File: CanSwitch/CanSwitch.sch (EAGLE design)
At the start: 17 parts

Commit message: #11 fixing RJ45 connector - connecting unused pins to +5V and GND
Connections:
- net +5V: now also RJ45CONNECTOR.RJ4515, RJ45CONNECTOR.RJ4517, RJ45CONNECTOR.RJ4525, RJ45CONNECTOR.RJ4527
- net GND: now also RJ45CONNECTOR.RJ4516, RJ45CONNECTOR.RJ4526
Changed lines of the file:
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@@
 <?xml version="1.0" encoding="utf-8"?>
 <!DOCTYPE eagle SYSTEM "eagle.dtd">
-<eagle version="7.6.0">
+<eagle version="7.7.0">
 <drawing>
 <settings>
@@
 <part name="STATUSLED" library="led" deviceset="LED" device="5MM"/>
 <part name="GND7" library="supply1" deviceset="GND" device=""/>
-<part name="GND1" library="supply1" deviceset="GND" device=""/>
 <part name="P+1" library="supply1" deviceset="+5V" device=""/>
 <part name="GND3" library="supply1" deviceset="GND" device=""/>
@@
 <instance part="STATUSLED" gate="G$1" x="-121.92" y="76.2" rot="R90"/>
 <instance part="GND7" gate="1" x="-134.62" y="76.2" rot="R270"/>
-<instance part="GND1" gate="1" x="-53.34" y="111.76"/>
 <instance part="P+1" gate="1" x="-27.94" y="91.44" rot="R90"/>
 <instance part="GND3" gate="1" x="-27.94" y="104.14" rot="R270"/>
@@
 </segment>
 <segment>
-<pinref part="RJ45CONNECTOR" gate="G$1" pin="RJ4519"/>
-<wire x1="-60.96" y1="119.38" x2="-55.88" y2="119.38" width="0.1524" layer="91"/>
-<label x="-60.96" y="116.84" size="1.778" layer="95"/>
-</segment>
-<segment>
 <pinref part="RJ45CONNECTOR" gate="G$1" pin="RJ4529"/>
 <wire x1="-20.32" y1="119.38" x2="-5.08" y2="119.38" width="0.1524" layer="91"/>
@@
 <wire x1="-48.26" y1="53.34" x2="-60.96" y2="53.34" width="0.1524" layer="91"/>
 <label x="-60.96" y="53.34" size="1.778" layer="95"/>
+</segment>
+<segment>
+<pinref part="RJ45CONNECTOR" gate="G$1" pin="RJ4515"/>
+<wire x1="-91.44" y1="119.38" x2="-104.14" y2="119.38" width="0.1524" layer="91"/>
+<label x="-106.68" y="119.38" size="1.778" layer="95"/>
+</segment>
+<segment>
+<pinref part="RJ45CONNECTOR" gate="G$1" pin="RJ4527"/>
+<wire x1="-20.32" y1="127" x2="-5.08" y2="127" width="0.1524" layer="91"/>
+<label x="-10.16" y="127" size="1.778" layer="95"/>
+</segment>
+<segment>
+<pinref part="RJ45CONNECTOR" gate="G$1" pin="RJ4517"/>
+<wire x1="-60.96" y1="127" x2="-58.42" y2="127" width="0.1524" layer="91"/>
+<label x="-63.5" y="124.46" size="1.778" layer="95"/>
+</segment>
+<segment>
+<pinref part="RJ45CONNECTOR" gate="G$1" pin="RJ4519"/>
+<pinref part="RJ45CONNECTOR" gate="G$1" pin="RJ4525"/>
+<wire x1="-60.96" y1="119.38" x2="-50.8" y2="119.38" width="0.1524" layer="91"/>
+<label x="-58.42" y="116.84" size="1.778" layer="95"/>
 </segment>
 </net>
@@
 </segment>
 <segment>
-<pinref part="RJ45CONNECTOR" gate="G$1" pin="RJ4518"/>
-<pinref part="RJ45CONNECTOR" gate="G$1" pin="RJ4524"/>
-<wire x1="-50.8" y1="121.92" x2="-53.34" y2="121.92" width="0.1524" layer="91"/>
-<pinref part="GND1" gate="1" pin="GND"/>
-<wire x1="-53.34" y1="121.92" x2="-60.96" y2="121.92" width="0.1524" layer="91"/>
-<wire x1="-53.34" y1="114.3" x2="-53.34" y2="121.92" width="0.1524" layer="91"/>
-<junction x="-53.34" y="121.92"/>
-</segment>
-<segment>
 <pinref part="DEBUGGING" gate="A" pin="3"/>
 <wire x1="-48.26" y1="50.8" x2="-60.96" y2="50.8" width="0.1524" layer="91"/>
 <label x="-60.96" y="50.8" size="1.778" layer="95"/>
+</segment>
+<segment>
+<pinref part="RJ45CONNECTOR" gate="G$1" pin="RJ4518"/>
+<pinref part="RJ45CONNECTOR" gate="G$1" pin="RJ4524"/>
+<wire x1="-50.8" y1="121.92" x2="-60.96" y2="121.92" width="0.1524" layer="91"/>
+<label x="-58.42" y="121.92" size="1.778" layer="95"/>
+</segment>
+<segment>
+<pinref part="RJ45CONNECTOR" gate="G$1" pin="RJ4526"/>
+<wire x1="-20.32" y1="129.54" x2="-5.08" y2="129.54" width="0.1524" layer="91"/>
+<label x="-10.16" y="129.54" size="1.778" layer="95"/>
+</segment>
+<segment>
+<pinref part="RJ45CONNECTOR" gate="G$1" pin="RJ4516"/>
+<wire x1="-60.96" y1="129.54" x2="-58.42" y2="129.54" width="0.1524" layer="91"/>
+<label x="-63.5" y="132.08" size="1.778" layer="95"/>
 </segment>
 </net>
@@
 <segment>
 <pinref part="RJ45CONNECTOR" gate="G$1" pin="RJ4522"/>
-<wire x1="-50.8" y1="129.54" x2="-58.42" y2="129.54" width="0.1524" layer="91"/>
-<label x="-58.42" y="132.08" size="1.778" layer="95"/>
+<wire x1="-50.8" y1="129.54" x2="-53.34" y2="129.54" width="0.1524" layer="91"/>
+<label x="-55.88" y="132.08" size="1.778" layer="95"/>
 </segment>
 </net>
@@
 <segment>
 <pinref part="RJ45CONNECTOR" gate="G$1" pin="RJ4523"/>
-<wire x1="-58.42" y1="127" x2="-50.8" y2="127" width="0.1524" layer="91"/>
-<label x="-58.42" y="124.46" size="1.778" layer="95"/>
-</segment>
-<segment>
+<wire x1="-53.34" y1="127" x2="-50.8" y2="127" width="0.1524" layer="91"/>
+<label x="-55.88" y="124.46" size="1.778" layer="95"/>
+</segment>
+<segment>

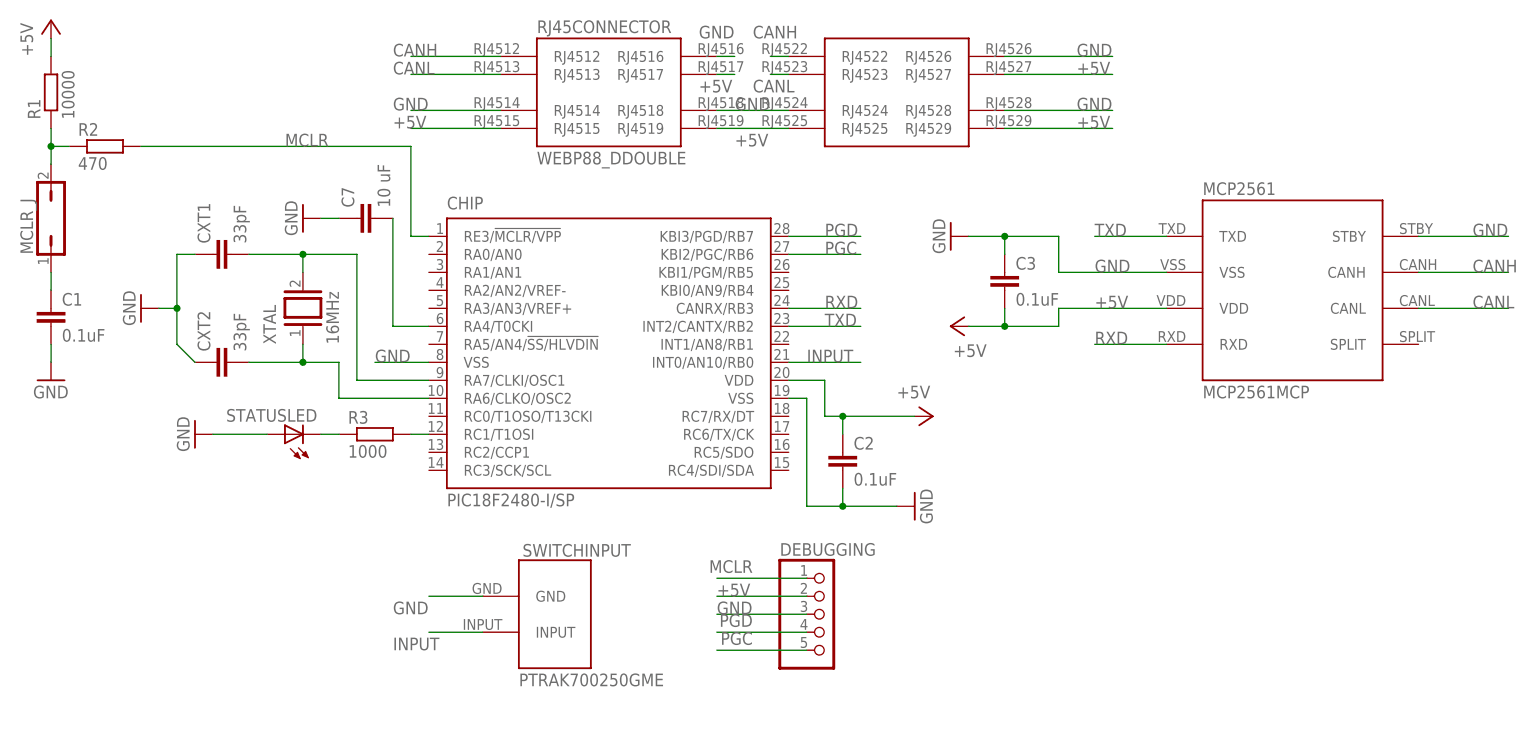
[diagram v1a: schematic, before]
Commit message: #13 connect RC3 of chip and STBY of transceiver, no route yet in board until the new inputs are added
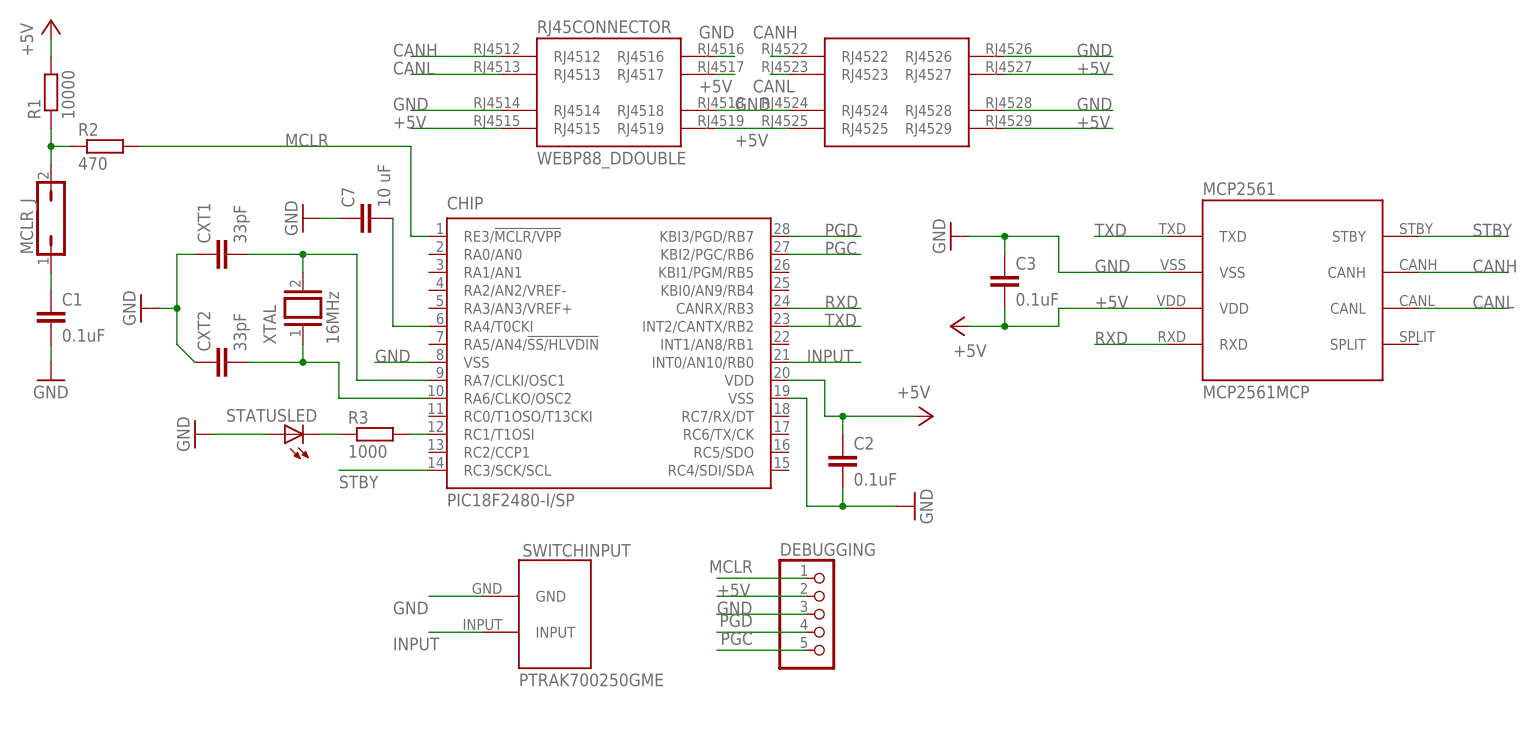
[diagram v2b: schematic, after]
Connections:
- new net STBY: CHIP.RC3/SCK/SCL, MCP2561.STBY
- net GND: no longer MCP2561.STBY
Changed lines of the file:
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@@
-</segment>
-<segment>
-<pinref part="MCP2561" gate="G$1" pin="STBY"/>
-<wire x1="38.1" y1="104.14" x2="50.8" y2="104.14" width="0.1524" layer="91"/>
-<label x="45.72" y="104.14" size="1.778" layer="95"/>
 </segment>
 <segment>
@@
 </segment>
 </net>
+<net name="STBY" class="0">
+<segment>
+<pinref part="MCP2561" gate="G$1" pin="STBY"/>
+<wire x1="38.1" y1="104.14" x2="50.8" y2="104.14" width="0.1524" layer="91"/>
+<label x="45.72" y="104.14" size="1.778" layer="95"/>
+</segment>
+<segment>
+<pinref part="CHIP" gate="G$1" pin="RC3/SCK/SCL"/>
+<wire x1="-101.6" y1="71.12" x2="-114.3" y2="71.12" width="0.1524" layer="91"/>
+<label x="-114.3" y="68.58" size="1.778" layer="95"/>
+</segment>
+</net>

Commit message: #8 support for 8 independent inputs  - dropped old switch input and replaced with RJ45 connector  - moved components around, moved transceiver down to the bottom and the  new RJ45 in the middle close to the chip  - re-routed related signals, made +5V thicker  - RX and TX routed to RC pins afterall, added labels too  - Eagle now reports clearance on the RJ45 socket, need to check allpcb  whether that is not too close for them to manufacter. probably is too  close, need to fix that next time
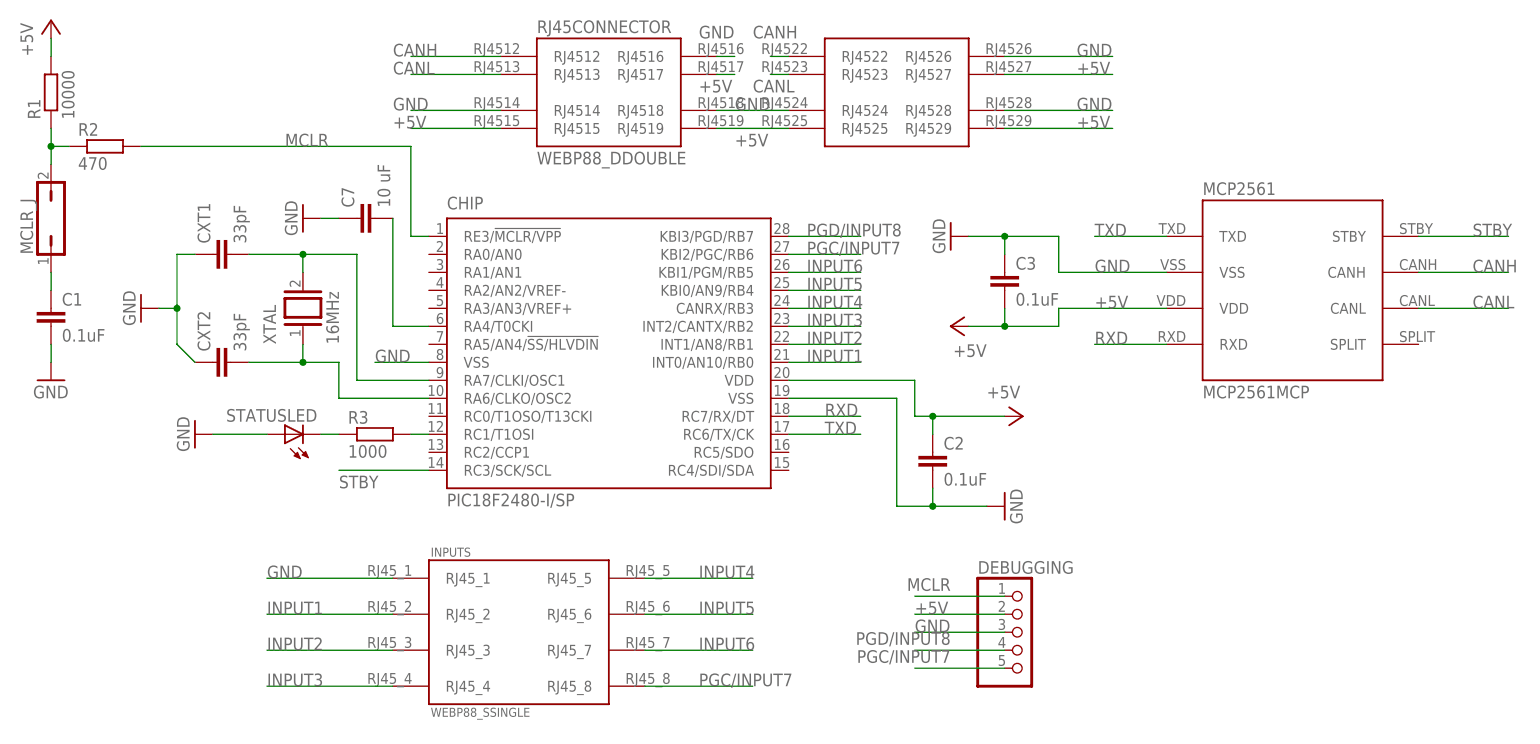
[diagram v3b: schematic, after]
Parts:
- removed SWITCHINPUT: PTRAK700250GME, PoJD:PTRAK700250GME
- added INPUTS: WEBP88_SSINGLE, PoJD:WEBP88_SSINGLE
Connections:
- net PGD renamed PGD/INPUT8
- removed net INPUT: CHIP.INT0/AN10/RB0, SWITCHINPUT.INPUT
- removed net PGC: CHIP.KBI2/PGC/RB6, DEBUGGING.5
- new net INPUT1: CHIP.INT0/AN10/RB0, INPUTS.RJ45_2
- new net INPUT2: CHIP.INT1/AN8/RB1, INPUTS.RJ45_3
- new net INPUT3: CHIP.INT2/CANTX/RB2, INPUTS.RJ45_4
- new net INPUT4: CHIP.CANRX/RB3, INPUTS.RJ45_5
- new net INPUT5: CHIP.KBI0/AN9/RB4, INPUTS.RJ45_6
- new net INPUT6: CHIP.KBI1/PGM/RB5, INPUTS.RJ45_7
- new net PGC/INPUT7: CHIP.KBI2/PGC/RB6, DEBUGGING.5, INPUTS.RJ45_8
- net GND: now also INPUTS.RJ45_1; no longer SWITCHINPUT.GND
- net RXD: now also CHIP.RC7/RX/DT; no longer CHIP.CANRX/RB3
- net TXD: now also CHIP.RC6/TX/CK; no longer CHIP.INT2/CANTX/RB2
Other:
- moved on the sheet: C2, DEBUGGING
